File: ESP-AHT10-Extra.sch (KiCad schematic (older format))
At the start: 26 parts, among them J1 USB, SW1 RESET, SW2 PROG, U1 CH330N, U2 HT7233, U3 ESP-12, U4 AHT10, U5 USBLC6-2SC6

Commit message: more notes on CH330N and 5V.
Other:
- note added: "NOTE: On paper, using 5V on VCC means\nwe drive TXD at 4.5V (well, 4.2V with\nthe drop from D1), which puts us above the\n3.6V specced working range. In practice,\nthe ESP-8266 is 5V tolerant on GPIO's.\n\nALSO NOTE: Apparently WCH\nchips have on-board USB\ntermination resistors."
- note removed: "NOTE: On paper, using 5V on VCC means\nwe drive TXD at 4.5V (well, 4.2V with\nthe drop from D1), which puts us above the\n3.6V max working range. 470R on TXD\nmight be a good idea. In practice, this\nseems to Just Work.\nALSO NOTE: Apparently WCH\nchips have on-board USB\ntermination resistors."
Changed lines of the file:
@@
 	10600 2850 10600 3000
 Text Notes 5800 5950 0    50   ~ 0
-NOTE: On paper, using 5V on VCC means\nwe drive TXD at 4.5V (well, 4.2V with\nthe drop from D1), which puts us above the\n3.6V max working range. 470R on TXD\nmight be a good idea. In practice, this\nseems to Just Work.\nALSO NOTE: Apparently WCH\nchips have on-board USB\ntermination resistors.
+NOTE: On paper, using 5V on VCC means\nwe drive TXD at 4.5V (well, 4.2V with\nthe drop from D1), which puts us above the\n3.6V specced working range. In practice,\nthe ESP-8266 is 5V tolerant on GPIO's.\n\nALSO NOTE: Apparently WCH\nchips have on-board USB\ntermination resistors.
 Wire Wire Line
 	8150 6050 9150 6050

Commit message: Connecting the CH330N to RESET is a bad idea when it's running on bus voltage.
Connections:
- net RESET: no longer U1.4 (~RTS)
- no-connect marks 5 -> 6
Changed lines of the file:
@@
 	1450 5200 1450 5900
 Connection ~ 1450 5900
-Text GLabel 9950 5750 2    50   Output ~ 0
-RESET
-Wire Wire Line
-	9550 5750 9950 5750
 Wire Notes Line
 	4450 7700 4450 550
 NoConn ~ 1750 6300
+NoConn ~ 9550 5750
 $EndSCHEMATC

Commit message: remove the RESET label
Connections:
- net RESET: no longer names the net of R2.2, SW1.1, U3.4 (GPIO16)
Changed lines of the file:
@@
 Text Notes 650  7600 0    50   ~ 0
 NOTE: R3 isn't needed for\nESP modules having an internal\nRESET pull-up. It'll still work if you\nadd it though.
-Text GLabel 1450 5200 1    50   Input ~ 0
-RESET
-Wire Wire Line
-	1450 5200 1450 5900
-Connection ~ 1450 5900
 Wire Notes Line
 	4450 7700 4450 550

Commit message: drop that extra 10uF cap. Aside from no longer being needed, this was probably keeping us beyond the USB spec.
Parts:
- removed C8: 10u, Capacitor_SMD:C_0805_2012Metric, symbol Device:C_Small
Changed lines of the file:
@@
 Wire Wire Line
 	1650 1350 1800 1350
-$Comp
-L Device:C_Small C8
-U 1 1 5DCC64D0
-P 7600 5150
-F 0 "C8" H 7692 5196 50  0000 L CNN
-F 1 "10u" H 7692 5105 50  0000 L CNN
-F 2 "Capacitor_SMD:C_0805_2012Metric" H 7600 5150 50  0001 C CNN
-F 3 "~" H 7600 5150 50  0001 C CNN
-	1    7600 5150
-	1    0    0    -1
-$EndComp
 Wire Wire Line
 	9150 4900 9150 5250
-Wire Wire Line
-	7450 4900 7600 4900
 Wire Wire Line
 	7950 5250 7950 6050
@@
 	7950 6050 8150 6050
 Connection ~ 8150 6050
-Wire Wire Line
-	7600 5250 7600 6050
-Wire Wire Line
-	7600 6050 7950 6050
-Connection ~ 7950 6050
-Wire Wire Line
-	7600 5050 7600 4900
-Connection ~ 7600 4900
-Wire Wire Line
-	7600 4900 7950 4900
 Wire Wire Line
 	7950 5050 7950 4900
@@
 NoConn ~ 1750 6300
 NoConn ~ 9550 5750
+Wire Wire Line
+	7450 4900 7950 4900
 $EndSCHEMATC

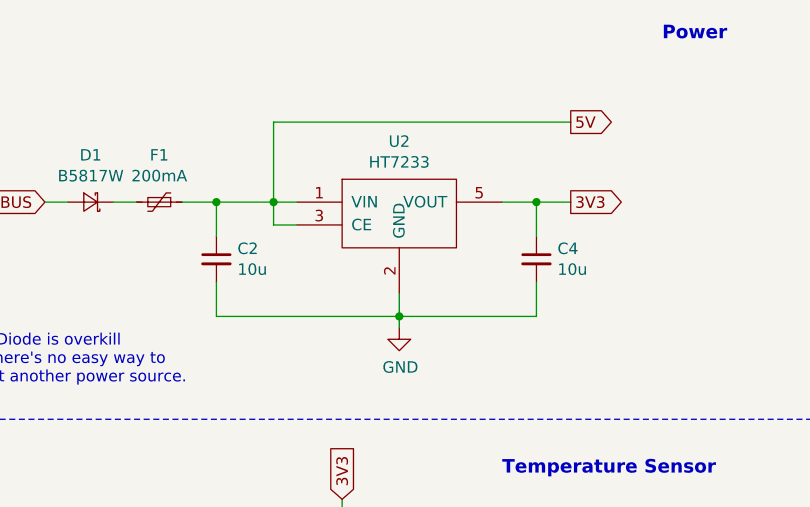
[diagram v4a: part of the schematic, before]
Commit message: cleanup some ground plane concerns swap to a SOT-23-3 footprint regulator bump rev to 1.5
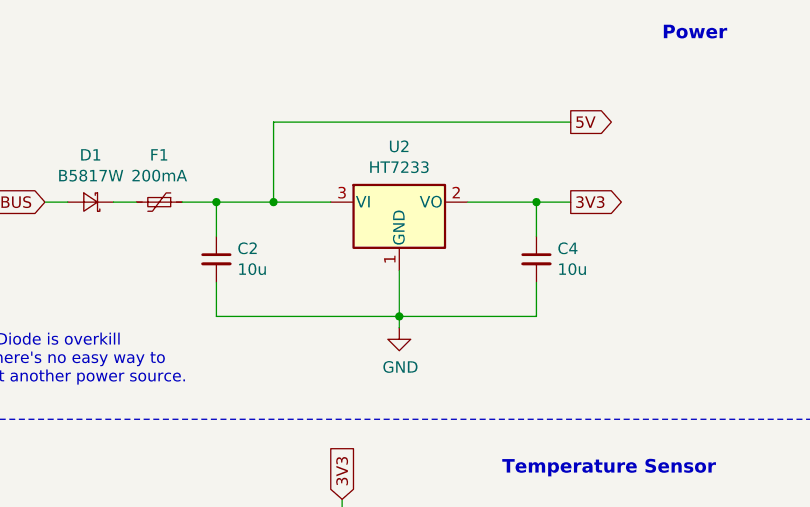
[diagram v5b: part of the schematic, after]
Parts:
- removed U2: HT7233, Package_TO_SOT_SMD:SOT-23-5, symbol Holtek:HT7233
- added U2: HT7233, Package_TO_SOT_SMD:SOT-23, symbol Regulator_Linear:MCP1700-3302E_SOT23
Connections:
- net 3V3: now also U2.2 (VO)
- net 5V: now also U2.3 (VI)
- net GND: now also U2.1 (GND)
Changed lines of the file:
@@
 Title ""
 Date ""
-Rev "1.4"
+Rev "1.5"
 Comp ""
 Comment1 ""
@@
 NoConn ~ 1750 6500
 NoConn ~ 3550 6400
-$Comp
-L Holtek:HT7233 U2
-U 1 1 5DBE1C35
-P 2600 1400
-F 0 "U2" H 2600 1715 50  0000 C CNN
-F 1 "HT7233" H 2600 1624 50  0000 C CNN
-F 2 "Package_TO_SOT_SMD:SOT-23-5" H 1900 1150 50  0001 C CNN
-F 3 "" H 2600 1550 50  0001 C CNN
-	1    2600 1400
-	1    0    0    -1
-$EndComp
-Wire Wire Line
-	2150 1450 2050 1450
-Wire Wire Line
-	2050 1450 2050 1350
 Connection ~ 2050 1350
-Wire Wire Line
-	2050 1350 2150 1350
 $Comp
 L Device:C_Small C2
@@
 	1    0    0    -1
 $EndComp
-Wire Wire Line
-	2600 1750 2600 1850
 Text GLabel 3350 1350 2    50   Output ~ 0
 3V3
-Wire Wire Line
-	3050 1350 3200 1350
 Wire Wire Line
 	3200 1350 3200 1500
@@
 Wire Wire Line
 	7450 4900 7950 4900
+$Comp
+L Regulator_Linear:MCP1700-3302E_SOT23 U2
+U 1 1 5E196253
+P 2600 1350
+F 0 "U2" H 2600 1592 50  0000 C CNN
+F 1 "HT7233" H 2600 1501 50  0000 C CNN
+F 2 "Package_TO_SOT_SMD:SOT-23" H 2600 1575 50  0001 C CNN
+F 3 "http://ww1.microchip.com/downloads/en/DeviceDoc/20001826C.pdf" H 2600 1350 50  0001 C CNN
+	1    2600 1350
+	1    0    0    -1
+$EndComp
+Wire Wire Line
+	2050 1350 2300 1350
+Wire Wire Line
+	2600 1650 2600 1850
+Wire Wire Line
+	2900 1350 3200 1350
 $EndSCHEMATC

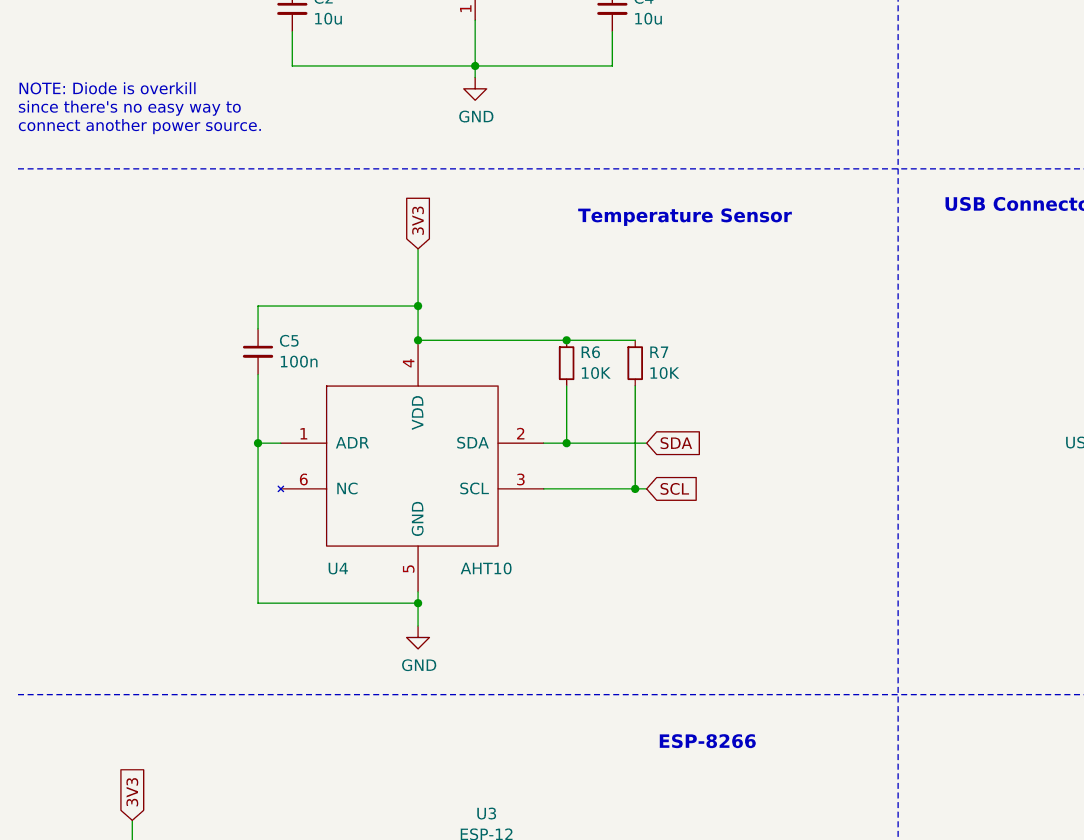
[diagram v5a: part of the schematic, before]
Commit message: Add a LTR-303 ambient light sensor
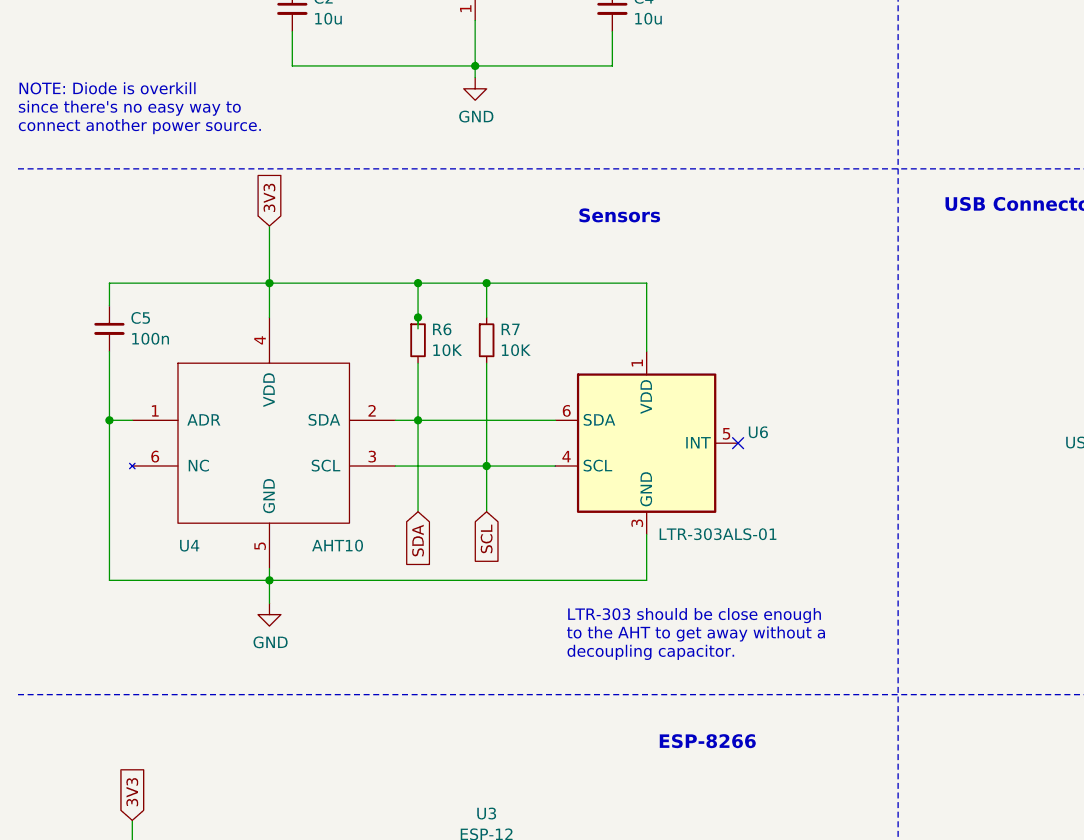
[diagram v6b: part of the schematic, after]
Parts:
- added U6: LTR-303ALS-01, CPB:Lite-On_LTR-303ALS-01_NoIntNoNc, symbol Sensor_Optical:LTR-303ALS-01
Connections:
- net 3V3: now also U6.1 (VDD)
- net GND: now also U6.3 (GND)
- net SCL: now also U6.4 (SCL)
- net SDA: now also U6.6 (SDA)
- no-connect marks 6 -> 7
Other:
- note added: "LTR-303 should be close enough\nto the AHT to get away without a\ndecoupling capacitor."
- note added: "Sensors"
- note removed: "Temperature Sensor"
- moved on the sheet: C5, R6, R7, U4
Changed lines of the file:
@@
 L AHT10:AHT10 U4
 U 1 1 5DBE6669
-P 2350 3600
-F 0 "U4" H 2000 3150 50  0000 C CNN
-F 1 "AHT10" H 2650 3150 50  0000 C CNN
-F 2 "CPB:AHT10-HandSolder" H 2350 3600 50  0001 C CNN
-F 3 "" H 2350 3600 50  0001 C CNN
-	1    2350 3600
-	1    0    0    -1
-$EndComp
-Text GLabel 3350 3700 2    50   Input ~ 0
+P 1700 3500
+F 0 "U4" H 1350 3050 50  0000 C CNN
+F 1 "AHT10" H 2000 3050 50  0000 C CNN
+F 2 "CPB:AHT10-HandSolder" H 1700 3500 50  0001 C CNN
+F 3 "" H 1700 3500 50  0001 C CNN
+	1    1700 3500
+	1    0    0    -1
+$EndComp
+Text GLabel 2650 3800 3    50   Input ~ 0
 SCL
-Text GLabel 3350 3500 2    50   Input ~ 0
+Text GLabel 2350 3800 3    50   Input ~ 0
 SDA
 Wire Wire Line
-	2900 3500 3000 3500
-Wire Wire Line
-	2900 3700 3300 3700
+	2250 3400 2350 3400
 $Comp
 L Device:R_Small R7
 U 1 1 5DBE999A
-P 3300 3150
-F 0 "R7" H 3359 3196 50  0000 L CNN
-F 1 "10K" H 3359 3105 50  0000 L CNN
-F 2 "Resistor_SMD:R_0805_2012Metric" H 3300 3150 50  0001 C CNN
-F 3 "~" H 3300 3150 50  0001 C CNN
-	1    3300 3150
+P 2650 3050
+F 0 "R7" H 2709 3096 50  0000 L CNN
+F 1 "10K" H 2709 3005 50  0000 L CNN
+F 2 "Resistor_SMD:R_0805_2012Metric" H 2650 3050 50  0001 C CNN
+F 3 "~" H 2650 3050 50  0001 C CNN
+	1    2650 3050
 	1    0    0    -1
 $EndComp
@@
 L Device:R_Small R6
 U 1 1 5DBE9A3C
-P 3000 3150
-F 0 "R6" H 3059 3196 50  0000 L CNN
-F 1 "10K" H 3059 3105 50  0000 L CNN
-F 2 "Resistor_SMD:R_0805_2012Metric" H 3000 3150 50  0001 C CNN
-F 3 "~" H 3000 3150 50  0001 C CNN
-	1    3000 3150
-	1    0    0    -1
-$EndComp
-Wire Wire Line
-	3300 3250 3300 3700
-Connection ~ 3300 3700
-Wire Wire Line
-	3300 3700 3350 3700
-Wire Wire Line
-	3000 3250 3000 3500
-Connection ~ 3000 3500
-Wire Wire Line
-	3000 3500 3350 3500
-Text GLabel 2350 2650 1    50   Input ~ 0
+P 2350 3050
+F 0 "R6" H 2409 3096 50  0000 L CNN
+F 1 "10K" H 2409 3005 50  0000 L CNN
+F 2 "Resistor_SMD:R_0805_2012Metric" H 2350 3050 50  0001 C CNN
+F 3 "~" H 2350 3050 50  0001 C CNN
+	1    2350 3050
+	1    0    0    -1
+$EndComp
+Wire Wire Line
+	2650 3150 2650 3600
+Connection ~ 2650 3600
+Wire Wire Line
+	2350 3150 2350 3400
+Connection ~ 2350 3400
+Text GLabel 1700 2550 1    50   Input ~ 0
 3V3
 $Comp
 L power:GND #PWR04
 U 1 1 5DBEAB2F
-P 2350 4300
-F 0 "#PWR04" H 2350 4050 50  0001 C CNN
-F 1 "GND" H 2355 4127 50  0000 C CNN
-F 2 "" H 2350 4300 50  0001 C CNN
-F 3 "" H 2350 4300 50  0001 C CNN
-	1    2350 4300
-	1    0    0    -1
-$EndComp
-Wire Wire Line
-	2350 2650 2350 2900
-Wire Wire Line
-	2350 3050 3000 3050
-Connection ~ 2350 3050
-Wire Wire Line
-	3000 3050 3300 3050
-Connection ~ 3000 3050
-Wire Wire Line
-	2350 4150 2350 4200
-Wire Wire Line
-	1750 3500 1650 3500
-Wire Wire Line
-	1650 3500 1650 4200
-Wire Wire Line
-	1650 4200 2350 4200
-Connection ~ 2350 4200
-Wire Wire Line
-	2350 4200 2350 4300
+P 1700 4200
+F 0 "#PWR04" H 1700 3950 50  0001 C CNN
+F 1 "GND" H 1705 4027 50  0000 C CNN
+F 2 "" H 1700 4200 50  0001 C CNN
+F 3 "" H 1700 4200 50  0001 C CNN
+	1    1700 4200
+	1    0    0    -1
+$EndComp
+Wire Wire Line
+	1700 2550 1700 2800
+Wire Wire Line
+	1700 4050 1700 4100
+Wire Wire Line
+	1100 3400 1000 3400
+Wire Wire Line
+	1000 3400 1000 4100
+Wire Wire Line
+	1000 4100 1700 4100
+Connection ~ 1700 4100
+Wire Wire Line
+	1700 4100 1700 4200
 $Comp
 L Device:C_Small C5
 U 1 1 5DBEEB4D
-P 1650 3100
-F 0 "C5" H 1742 3146 50  0000 L CNN
-F 1 "100n" H 1742 3055 50  0000 L CNN
-F 2 "Capacitor_SMD:C_0805_2012Metric" H 1650 3100 50  0001 C CNN
-F 3 "~" H 1650 3100 50  0001 C CNN
-	1    1650 3100
-	1    0    0    -1
-$EndComp
-Wire Wire Line
-	1650 3200 1650 3500
-Connection ~ 1650 3500
-Wire Wire Line
-	1650 3000 1650 2900
-Wire Wire Line
-	1650 2900 2350 2900
-Connection ~ 2350 2900
-Wire Wire Line
-	2350 2900 2350 3050
+P 1000 3000
+F 0 "C5" H 1092 3046 50  0000 L CNN
+F 1 "100n" H 1092 2955 50  0000 L CNN
+F 2 "Capacitor_SMD:C_0805_2012Metric" H 1000 3000 50  0001 C CNN
+F 3 "~" H 1000 3000 50  0001 C CNN
+	1    1000 3000
+	1    0    0    -1
+$EndComp
+Wire Wire Line
+	1000 3100 1000 3400
+Connection ~ 1000 3400
+Wire Wire Line
+	1000 2900 1000 2800
+Wire Wire Line
+	1000 2800 1700 2800
+Connection ~ 1700 2800
+Wire Wire Line
+	1700 2800 1700 2950
 $Comp
 L Device:R_Small R3
@@
 USB Controller
 Text Notes 3050 2550 0    59   ~ 12
-Temperature Sensor
+Sensors
 Text Notes 3400 4850 0    59   ~ 12
 ESP-8266
@@
 Wire Wire Line
 	2900 1350 3200 1350
+$Comp
+L Sensor_Optical:LTR-303ALS-01 U6
+U 1 1 5E1A5ABC
+P 3350 3500
+F 0 "U6" H 3791 3546 50  0000 L CNN
+F 1 "LTR-303ALS-01" H 3400 3100 50  0000 L CNN
+F 2 "CPB:Lite-On_LTR-303ALS-01_NoIntNoNc" H 3350 3950 50  0001 C CNN
+F 3 "http://optoelectronics.liteon.com/upload/download/DS86-2013-0004/LTR-303ALS-01_DS_V1.pdf" H 3050 3850 50  0001 C CNN
+	1    3350 3500
+	1    0    0    -1
+$EndComp
+Wire Wire Line
+	2650 3600 2950 3600
+Wire Wire Line
+	2350 3400 2950 3400
+Wire Wire Line
+	2250 3600 2650 3600
+Wire Wire Line
+	2650 3800 2650 3600
+Wire Wire Line
+	2350 3800 2350 3400
+Wire Wire Line
+	1700 4100 3350 4100
+Wire Wire Line
+	3350 4100 3350 3900
+NoConn ~ 3750 3500
+Wire Wire Line
+	1700 2800 2350 2800
+Wire Wire Line
+	3350 2800 3350 3100
+Wire Wire Line
+	2650 2950 2650 2800
+Connection ~ 2650 2800
+Wire Wire Line
+	2650 2800 3350 2800
+Wire Wire Line
+	2350 3000 2350 2950
+Connection ~ 2350 2800
+Wire Wire Line
+	2350 2800 2650 2800
+Connection ~ 2350 2950
+Wire Wire Line
+	2350 2950 2350 2800
+Text Notes 3000 4450 0    50   ~ 0
+LTR-303 should be close enough\nto the AHT to get away without a\ndecoupling capacitor.
 $EndSCHEMATC

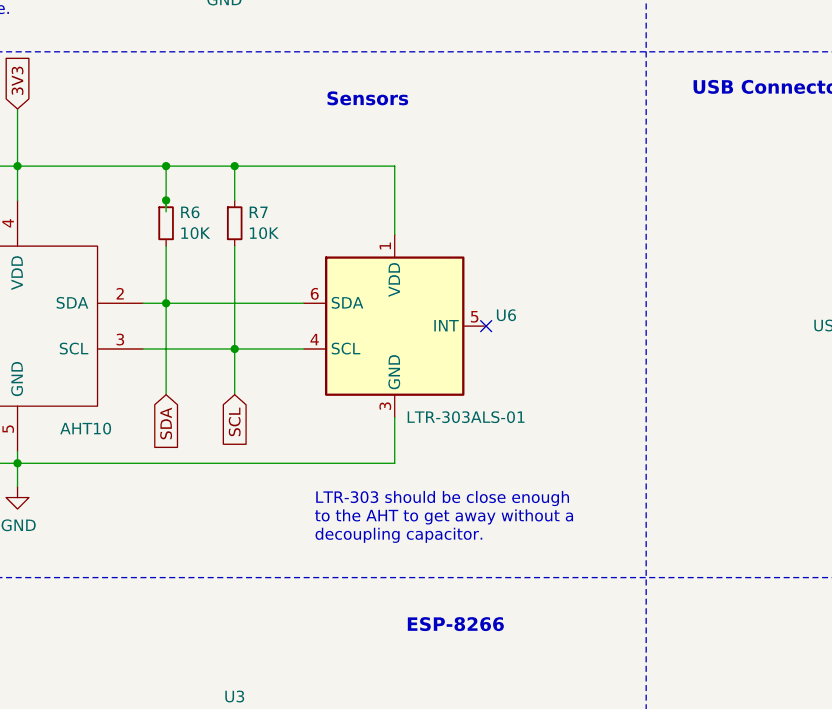
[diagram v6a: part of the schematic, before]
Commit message: switch the ALS to the VEML7700. Seems a lot less flaky, but a *lot* bigger.
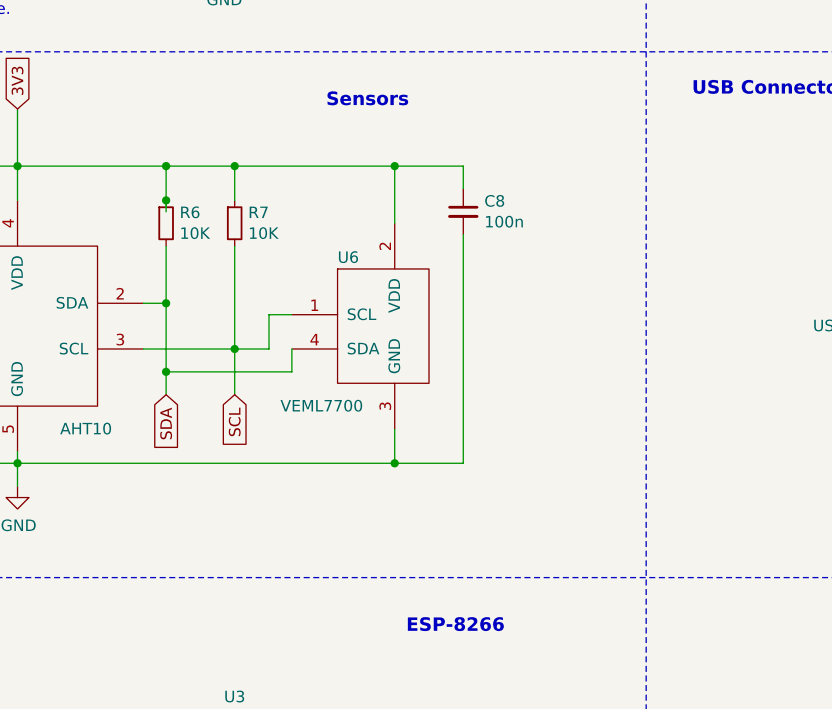
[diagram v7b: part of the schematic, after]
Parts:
- removed U6: LTR-303ALS-01, CPB:Lite-On_LTR-303ALS-01_NoIntNoNc, symbol Sensor_Optical:LTR-303ALS-01
- added C8: 100n, Capacitor_SMD:C_0805_2012Metric, symbol Device:C_Small
- added U6: VEML7700, CPB:VEML7700, symbol VEML7700:VEML7700
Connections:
- net 3V3: now also C8.1, U6.2 (VDD)
- net GND: now also C8.2, U6.3 (GND)
- net SCL: now also U6.1 (SCL)
- net SDA: now also U6.4 (SDA)
- no-connect marks 7 -> 6
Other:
- note removed: "LTR-303 should be close enough\nto the AHT to get away without a\ndecoupling capacitor."
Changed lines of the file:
@@
 Wire Wire Line
 	2900 1350 3200 1350
-$Comp
-L Sensor_Optical:LTR-303ALS-01 U6
-U 1 1 5E1A5ABC
-P 3350 3500
-F 0 "U6" H 3791 3546 50  0000 L CNN
-F 1 "LTR-303ALS-01" H 3400 3100 50  0000 L CNN
-F 2 "CPB:Lite-On_LTR-303ALS-01_NoIntNoNc" H 3350 3950 50  0001 C CNN
-F 3 "http://optoelectronics.liteon.com/upload/download/DS86-2013-0004/LTR-303ALS-01_DS_V1.pdf" H 3050 3850 50  0001 C CNN
-	1    3350 3500
-	1    0    0    -1
-$EndComp
-Wire Wire Line
-	2650 3600 2950 3600
-Wire Wire Line
-	2350 3400 2950 3400
 Wire Wire Line
 	2250 3600 2650 3600
@@
 	2650 3800 2650 3600
 Wire Wire Line
-	2350 3800 2350 3400
+	2350 3800 2350 3700
 Wire Wire Line
 	1700 4100 3350 4100
 Wire Wire Line
-	3350 4100 3350 3900
-NoConn ~ 3750 3500
-Wire Wire Line
 	1700 2800 2350 2800
-Wire Wire Line
-	3350 2800 3350 3100
 Wire Wire Line
 	2650 2950 2650 2800
@@
 Wire Wire Line
 	2350 2950 2350 2800
-Text Notes 3000 4450 0    50   ~ 0
-LTR-303 should be close enough\nto the AHT to get away without a\ndecoupling capacitor.
+$Comp
+L VEML7700:VEML7700 U6
+U 1 1 5E6B90B2
+P 3350 3500
+F 0 "U6" H 3100 3800 50  0000 L CNN
+F 1 "VEML7700" H 2850 3150 50  0000 L CNN
+F 2 "CPB:VEML7700" H 3100 3700 50  0001 C CNN
+F 3 "http://www.vishay.com/docs/84286/veml7700.pdf" H 3200 3800 50  0001 C CNN
+	1    3350 3500
+	1    0    0    -1
+$EndComp
+Wire Wire Line
+	3350 2800 3350 3050
+Wire Wire Line
+	3350 3950 3350 4100
+Wire Wire Line
+	2900 3450 2800 3450
+Wire Wire Line
+	2800 3450 2800 3600
+Wire Wire Line
+	2800 3600 2650 3600
+Wire Wire Line
+	2900 3600 2900 3700
+Wire Wire Line
+	2900 3700 2350 3700
+Connection ~ 2350 3700
+Wire Wire Line
+	2350 3700 2350 3400
+$Comp
+L Device:C_Small C8
+U 1 1 5E6C6864
+P 3650 3000
+F 0 "C8" H 3742 3046 50  0000 L CNN
+F 1 "100n" H 3742 2955 50  0000 L CNN
+F 2 "Capacitor_SMD:C_0805_2012Metric" H 3650 3000 50  0001 C CNN
+F 3 "~" H 3650 3000 50  0001 C CNN
+	1    3650 3000
+	1    0    0    -1
+$EndComp
+Wire Wire Line
+	3650 2800 3650 2900
+Wire Wire Line
+	3350 2800 3650 2800
+Connection ~ 3350 2800
+Wire Wire Line
+	3650 3100 3650 4100
+Wire Wire Line
+	3650 4100 3350 4100
+Connection ~ 3350 4100
 $EndSCHEMATC
